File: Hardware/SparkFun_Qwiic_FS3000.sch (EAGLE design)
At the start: 26 parts, among them J2 QWIIC_RA, U1 FS3000

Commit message: Layout done
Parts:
- LOGO2: value SFE_LOGO_NAME_FLAME.1_INCH -> SFE_LOGO_FLAME.1_INCH; device SparkFun-Aesthetics:SFE_LOGO_NAME_FLAME.1_INCH -> SparkFun-Aesthetics:SFE_LOGO_FLAME.1_INCH
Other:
- moved on the sheet: J1, J2, J5

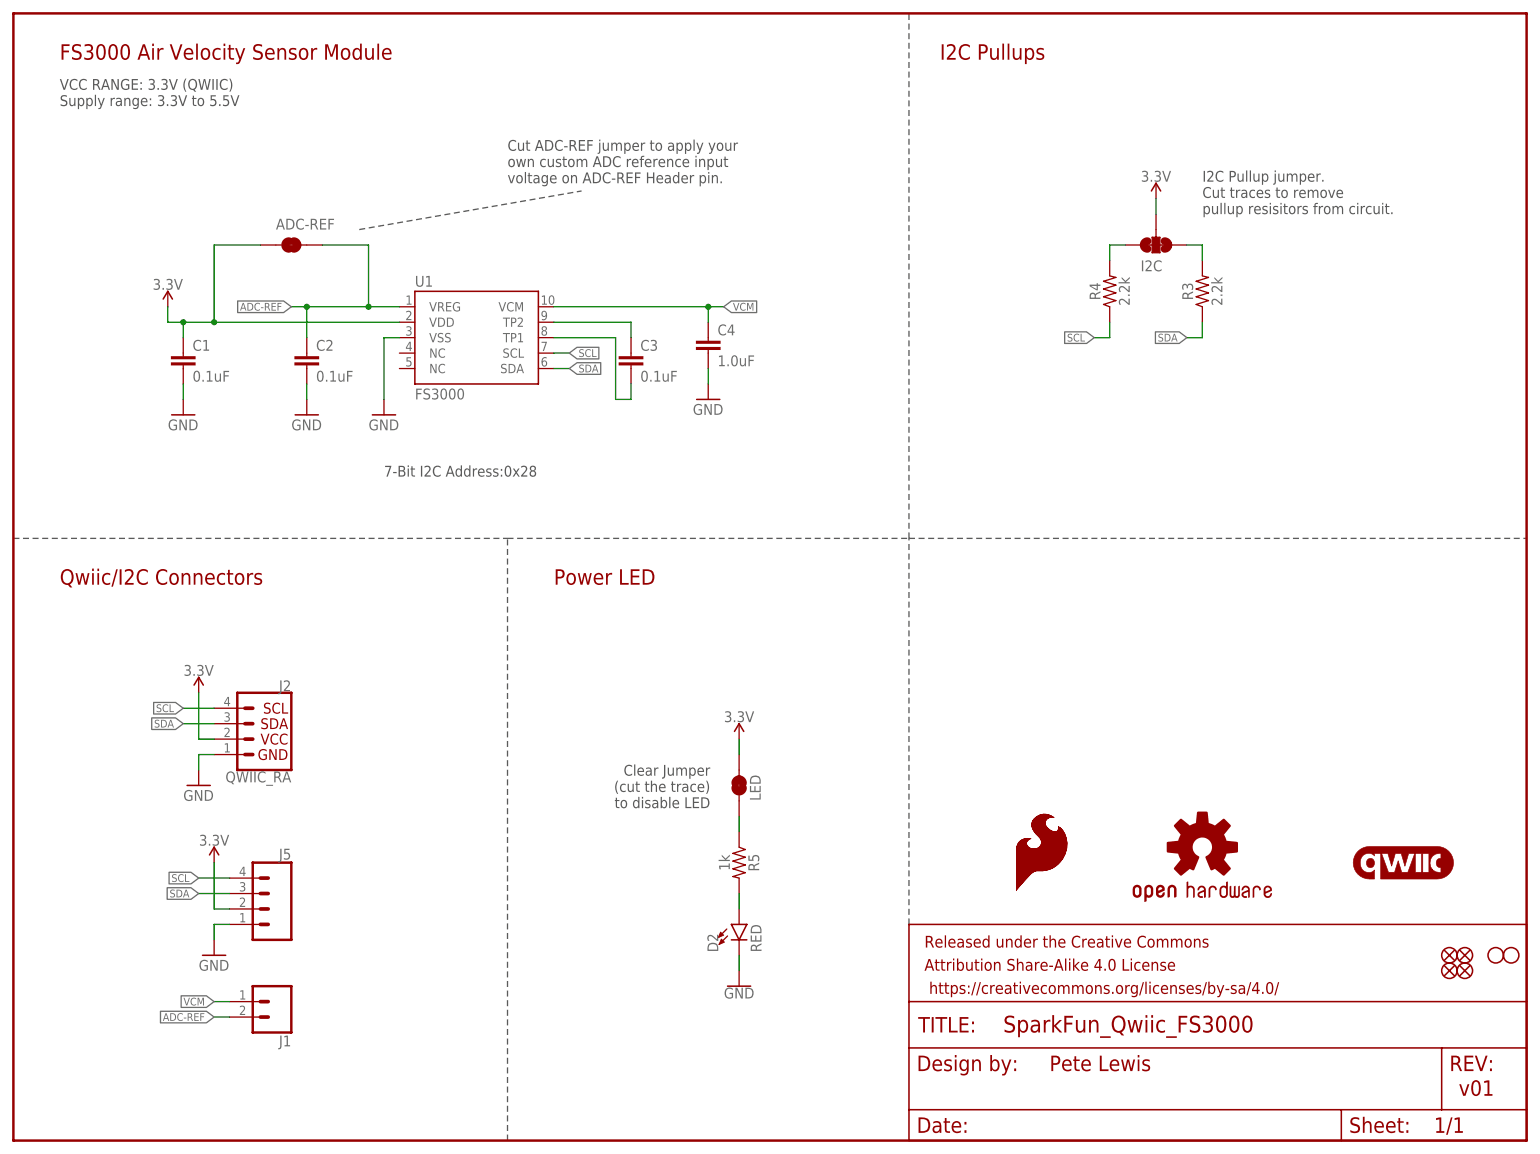
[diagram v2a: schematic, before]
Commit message: Group Review Changes
-Buzzard labels on VCM/ADCR changed to be correct inputs/outputs end type
-Added in solder pads for two versions (7.23m/s vs 15m/s) (1005/1015)
-Moved"supply range" to below the IC and change to "VDD range".
-schematic cleanup - power LED jumper paragraph. space in I2C address.
-added space between "I2C address" and "0x28" in board silk
-added name/flame logo to board silk.
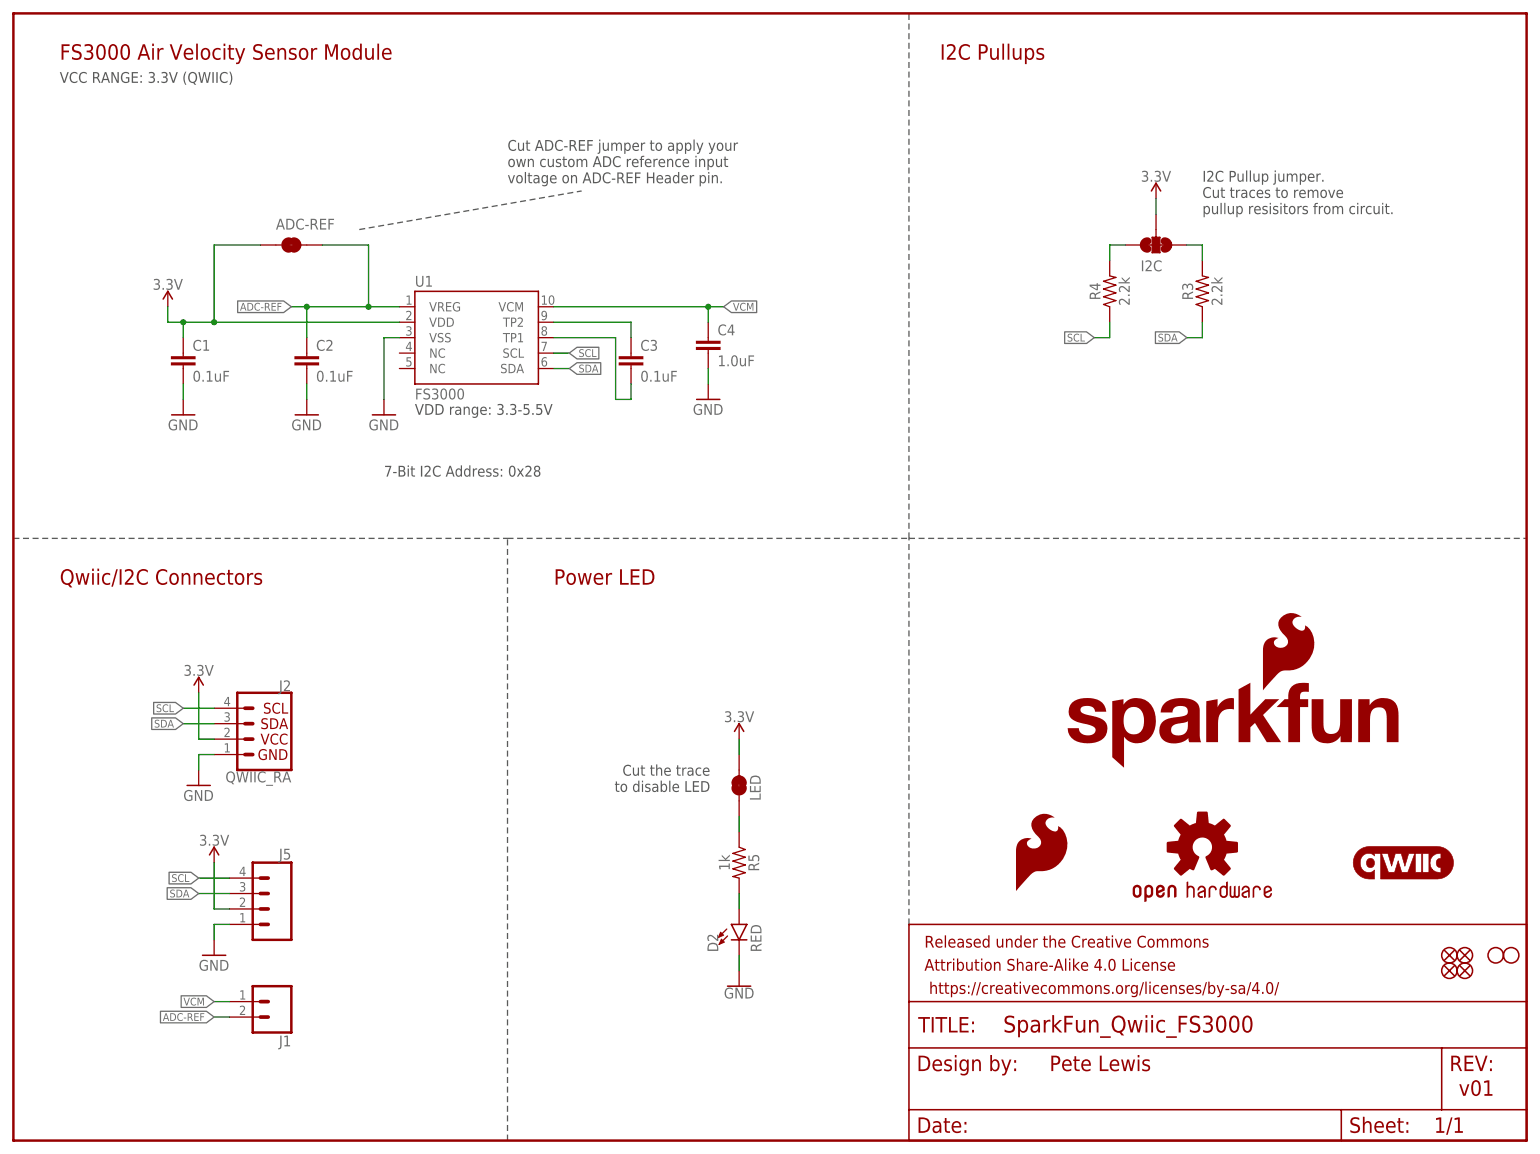
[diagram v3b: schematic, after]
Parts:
- removed LOGO2: SFE_LOGO_FLAME.1_INCH, SparkFun-Aesthetics:SFE_LOGO_FLAME.1_INCH
- added LOGO5: SFE_LOGO_NAME_FLAME.1_INCH, SparkFun-Aesthetics:SFE_LOGO_NAME_FLAME.1_INCH
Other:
- note added: "7-Bit I2C Address: 0x28"
- note added: "Cut the trace to disable LED"
- note added: "VCC RANGE: 3.3V (QWIIC)"
- note added: "VDD range: 3.3-5.5V"
- note removed: "7-Bit I2C Address:0x28"
- note removed: "Clear Jumper (cut the trace) to disable LED"
- note removed: "VCC RANGE: 3.3V (QWIIC) Supply range: 3.3V to 5.5V"
